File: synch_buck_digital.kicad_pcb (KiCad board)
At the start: 4 copper layers, 52.8 x 49.6 mm, 49 parts, among them U1 BSC066N06NSATMA1, U2 BSC066N06NSATMA1, U3 INA241A3IDDFR

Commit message: Small Changes
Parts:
- moved D1 0.76 mm to (230.2, 92.7)
- moved C_DT_10N1 0.35 mm to (198.0, 81.1)
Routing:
- net /V_FB: track 39.9 -> 39.0 mm
- net /PWM_LS: track 33.9 -> 33.0 mm

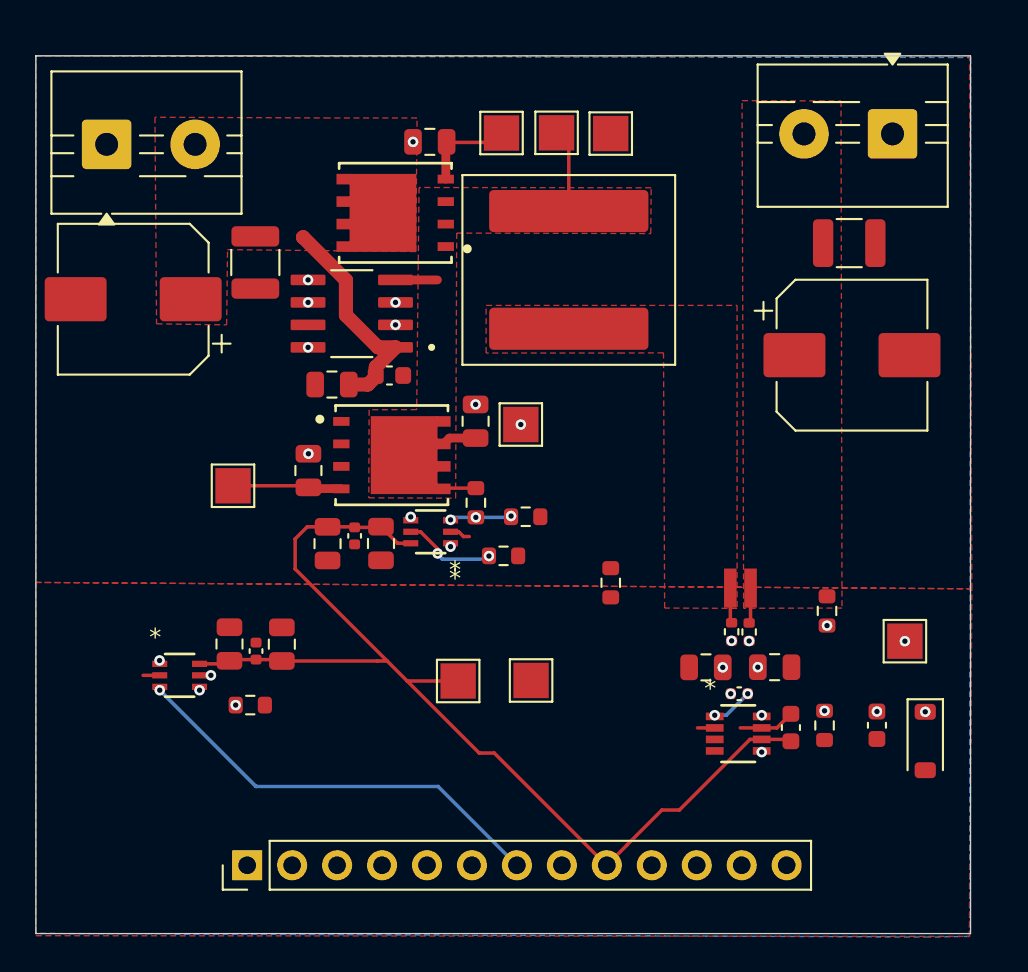
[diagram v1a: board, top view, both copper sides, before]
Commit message: Added stitching and thermal pours
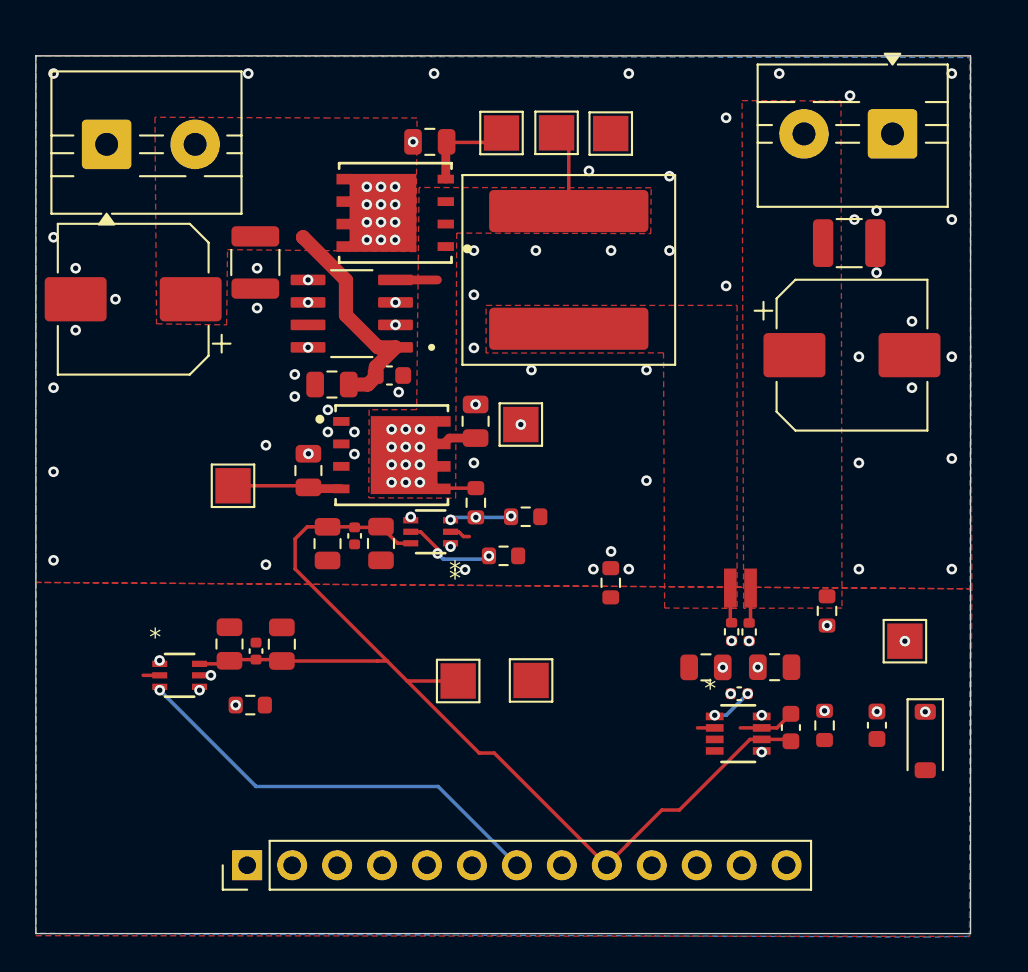
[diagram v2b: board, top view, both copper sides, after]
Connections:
- J_STM1 pad 3: /PWM_LS -> /PWM_HS
- J_STM1 pad 4: /PWM_HS -> /PWM_LS
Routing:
- net /PWM_LS: track 33.0 -> 34.7 mm
- net PGND: vias 0 -> 55
- net /SW: vias 0 -> 12
- net +12V: vias 0 -> 12

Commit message: Small fix
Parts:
- moved R1_DT1 2.89 mm to (204.9, 79.4), turned to 90 degrees
- moved R2_DT1 1.74 mm to (206.6, 79.4)
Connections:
- R1_DT1 pad 2: PGND -> /SW
- R2_DT1 pad 1: /SW -> PGND

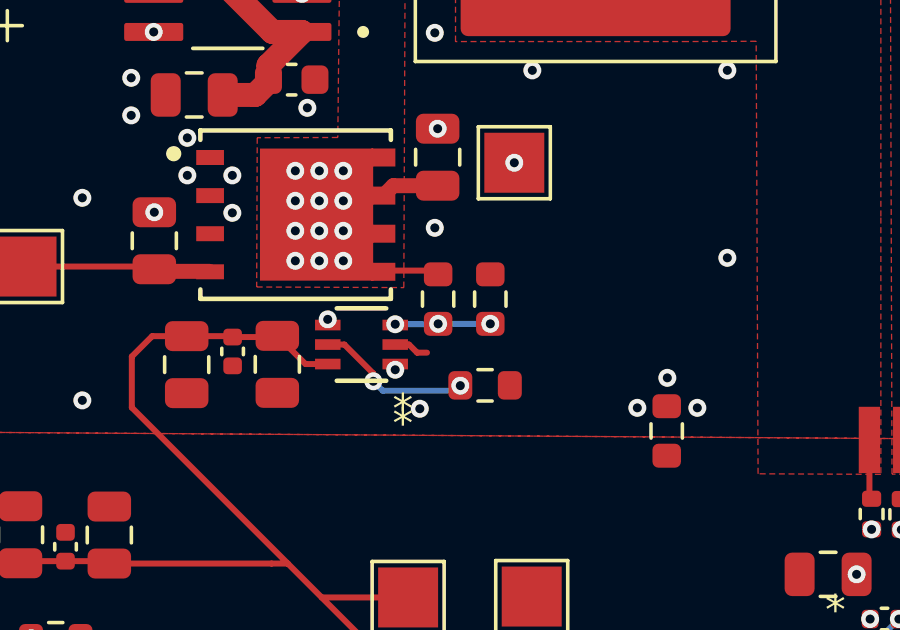
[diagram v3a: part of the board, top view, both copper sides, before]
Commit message: Small layout fix
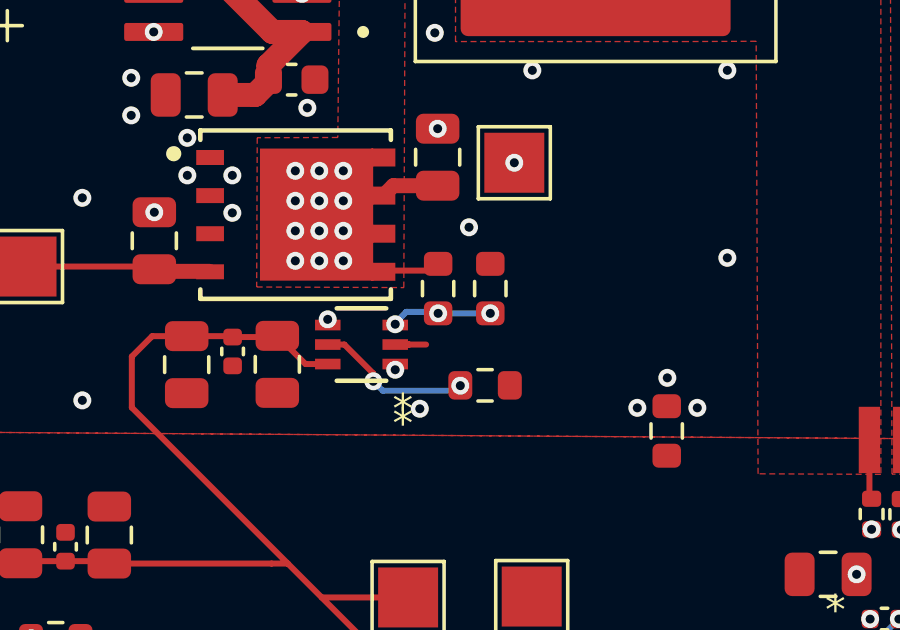
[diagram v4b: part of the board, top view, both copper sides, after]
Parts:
- moved R1_DT1 0.35 mm to (204.9, 79.0)
- moved R2_DT1 0.35 mm to (206.6, 79.0)

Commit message: V1 finished. Final touchups to schematic planned
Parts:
- U1, U2: footprint FET:PG-TDSON-8_INF -> Package_SON:Infineon_PG-TDSON-8_6.15x5.15mm
- moved U2 0.07 mm to (200.2, 62.9)
